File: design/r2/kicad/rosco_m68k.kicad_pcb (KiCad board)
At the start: 4 copper layers, 160 x 100 mm, 84 parts, among them IC1 MC68010P10, IC2 ATF16V8BQL-15PU, IC3 ATF16V8BQL-15PU, IC4 MC68901P, IC5 ATF16V8BQL-15PU, IC6 74174N, IC7 74LS93, IC8 555N, IC9 74LS01N, J1 PWR, J2 Conn_01x06, J3 Conn_02x32_Odd_Even, J4 Conn_01x06, J5 GPIO-PANEL, Q1 3.6864MHz, Q2 5H8ET-10.000, Q3 5H8ET-4.000, U1 AT28C256-15PU, U2 AT28C256-15PU, U3 AS6C4008-55PCN, U4 AS6C4008-55PCN

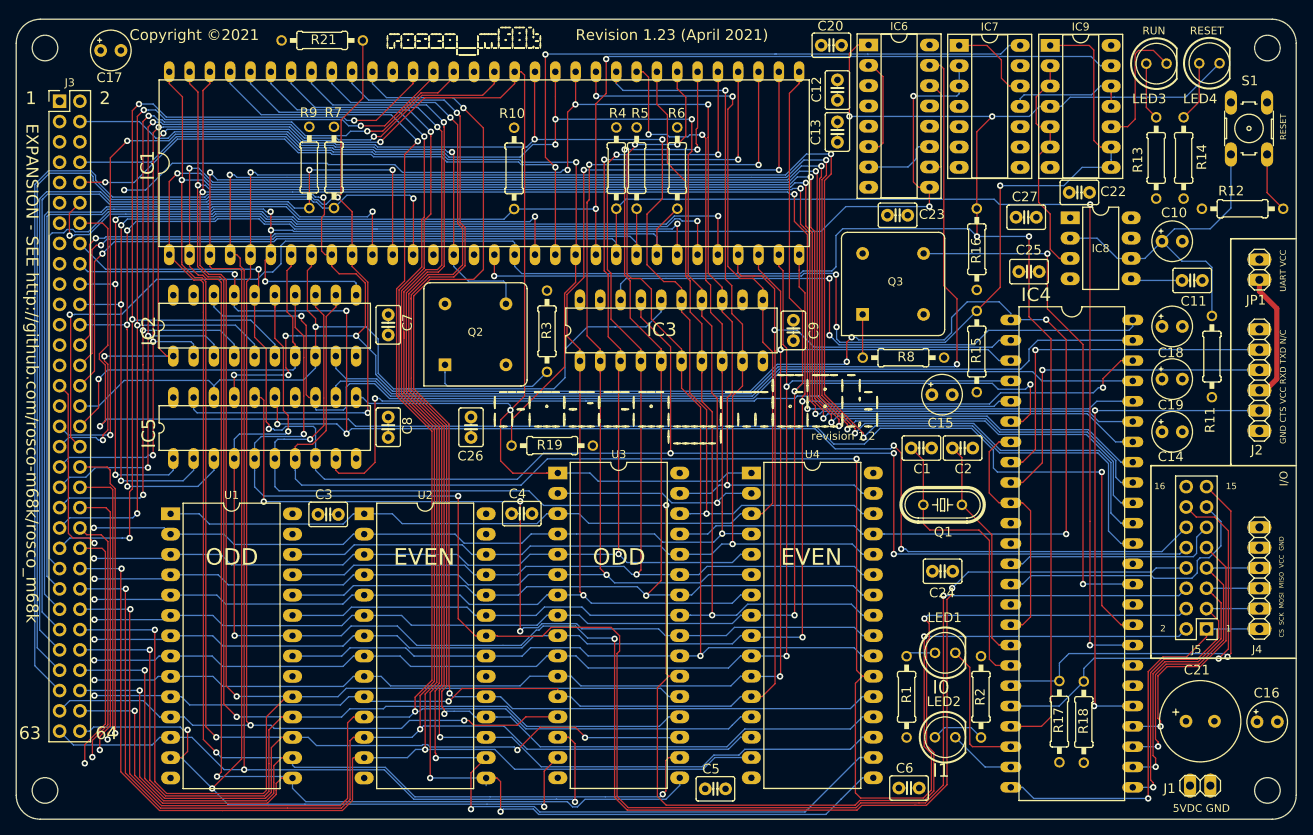
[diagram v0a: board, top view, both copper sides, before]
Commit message: Schematic / GAL tweaks and do layout
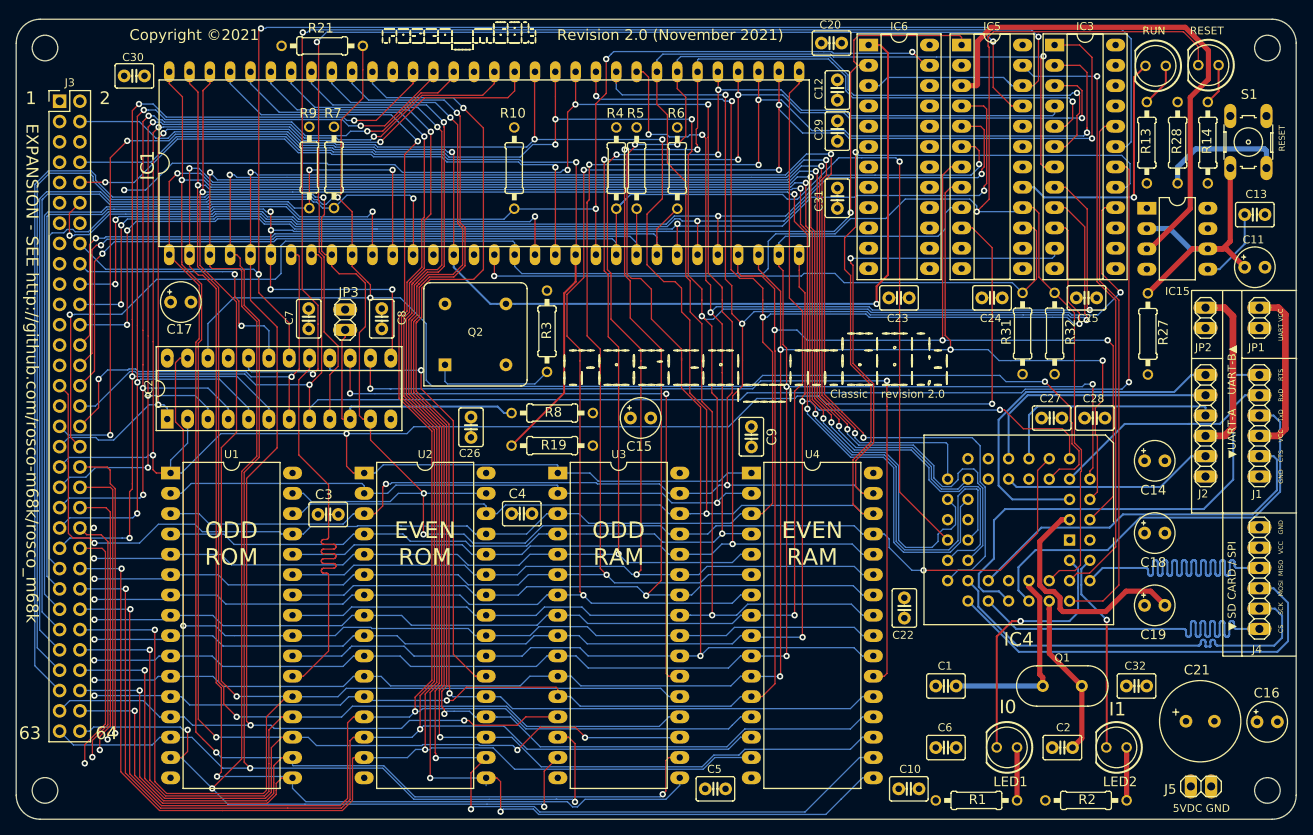
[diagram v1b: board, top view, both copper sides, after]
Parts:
- removed IC7: 74LS93, Package_DIP:DIP-14_W7.62mm_Socket_LongPads
- removed IC8: 555N, Package_DIP:DIP-8_W7.62mm_LongPads
- removed IC9: 74LS01N, Package_DIP:DIP-14_W7.62mm_Socket_LongPads
- removed the LED3 at (210.4, 60.6)
- removed the LED4 at (217.1, 60.6)
- removed Q3: 5H8ET-4.000, Oscillator:Oscillator_DIP-8
- removed R11: 2K2, rosco_m68k:0207_10
- removed R12: 270R, rosco_m68k:0207_10
- removed R15, R16, R17, R18: 4K7, rosco_m68k:0207_10
- removed the REF** at (92.2, 76.3)
- removed the REF** at (153.7, 104.2)
- added C28: 100nF, rosco_m68k:C2.5-3, F.Cu at (202.7, 105.0)
- added C29: 100nF, rosco_m68k:C2.5-3, F.Cu at (170.6, 69.1)
- added C30: 100nF, rosco_m68k:C2.5-3, F.Cu at (82.7, 62.2)
- added C31: 100nF, rosco_m68k:C2.5-3, F.Cu at (170.6, 77.5)
- added C32: 100nF, rosco_m68k:C2.5-3, F.Cu at (207.9, 138.4)
- added IC15: 555N, Package_DIP:DIP-8_W7.62mm_LongPads, F.Cu at (209.2, 78.7)
- added JP2: Jumper, rosco_m68k:1X02, F.Cu at (216.6, 92.4)
- added JP3: Jumper, rosco_m68k:1X02, F.Cu at (109.0, 92.7)
- added LED1: GREEN, rosco_m68k:LED5MM, F.Cu at (191.7, 146.1)
- added LED2: RED, rosco_m68k:LED5MM, F.Cu at (205.4, 146.1)
- added R27: 2K2, rosco_m68k:0207_10, F.Cu at (209.4, 94.4)
- added R28: 270R, rosco_m68k:0207_10, F.Cu at (213.1, 70.5)
- added R31: 4K7, rosco_m68k:0207_10, F.Cu at (193.7, 94.4)
- added R32: 4K7, rosco_m68k:0207_10, F.Cu at (197.7, 94.4)
- added REF**: WEEE-Logo_5.6x8mm_SilkScreen, Symbol:WEEE-Logo_5.6x8mm_SilkScreen, B.Cu at (92.2, 76.9)
- C1, C2: value 33pF -> 7pF
- C10: value 100uF -> 100nF; footprint rosco_m68k:E2,5-5 -> rosco_m68k:C2.5-3
- C11: value 100nF -> 100uF; footprint rosco_m68k:C2.5-3 -> rosco_m68k:E2,5-5
- IC2, IC5: footprint rosco_m68k:DIL20 -> Package_DIP:DIP-24_W7.62mm_Socket_LongPads
- IC3: value ATF16V8BQL-15PU -> ATF22V10C; footprint rosco_m68k:DIL20 -> Package_DIP:DIP-24_W7.62mm_Socket_LongPads
- IC4: value MC68901P -> XR68C681CJTR-F; footprint rosco_m68k:DIL48 -> Package_LCC:PLCC-44_THT-Socket
- IC6: value 74174N -> ATF22V10C; footprint Package_DIP:DIP-16_W7.62mm_Socket_LongPads -> Package_DIP:DIP-24_W7.62mm_Socket_LongPads
- J1: value PWR -> UART_A; footprint rosco_m68k:1X02 -> rosco_m68k:1X06
- J2: value Conn_01x06 -> UART_B
- J5: value GPIO-PANEL -> PWR; footprint Connector_PinHeader_2.54mm:PinHeader_2x08_P2.54mm_Vertical -> rosco_m68k:1X02
- JP1: value FTDI POWER -> Jumper
- Q1: value 3.6864MHz -> Crystal; footprint rosco_m68k:HC49_S -> Crystal:Crystal_HC49-4H_Vertical
- R21: value 2K2 -> 1K2
- U1, U2: value AT28C256-15PU -> SST39SF040; footprint Package_DIP:DIP-28_W15.24mm_LongPads -> Package_DIP:DIP-32_W15.24mm_LongPads
- moved IC5 99.4 mm to (186.1, 58.3)
- moved LED4 90.2 mm to (216.9, 60.8), turned to 180 degrees
- moved LED3 77.9 mm to (210.3, 60.9), turned to 180 degrees
- moved C10 76.0 mm to (179.5, 151.3), turned to 180 degrees
- moved IC3 59.7 mm to (197.7, 58.3)
- moved C22 56.4 mm to (178.9, 128.7), turned to 90 degrees
- moved C13 53.2 mm to (222.7, 79.5), turned to 180 degrees
- moved R8 44.4 mm to (134.9, 104.3)
- moved J1 43.1 mm to (223.3, 108.4), turned to 90 degrees
- moved C2 39.5 mm to (198.7, 146.1), turned to 180 degrees
- moved C15 37.8 mm to (145.9, 104.9)
- moved C24 34.7 mm to (189.9, 89.9)
- moved C17 32.6 mm to (88.5, 90.5)
- moved C1 29.9 mm to (184.1, 138.4)
- moved C19 28.4 mm to (210.2, 128.4)
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- renumbered LED1 to LED3, LED2 to LED4
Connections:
- net /Expansion/A20 renamed A20
- net /Expansion/A21 renamed A21
- net /Expansion/A22 renamed A22
- net /Expansion/A23 renamed A23
- C1 pad 1: Net-(C1-Pad1) -> GND
- C1 pad 2: GND -> Net-(C1-Pad2)
- C13 pad 2: GND -> Net-(C13-Pad2)
- IC1 pad 1: /Expansion/D4 -> D4
- IC1 pad 2: /Expansion/D3 -> D3
- IC1 pad 29: /Expansion/A1 -> A1
- IC1 pad 3: /Expansion/D2 -> D2
- IC1 pad 30: /Expansion/A2 -> A2
- IC1 pad 31: /Expansion/A3 -> A3
- IC1 pad 32: /Expansion/A4 -> A4
- IC1 pad 33: /Expansion/A5 -> A5
- IC1 pad 34: /Expansion/A6 -> A6
- IC1 pad 35: /Expansion/A7 -> A7
- IC1 pad 36: /Expansion/A8 -> A8
- IC1 pad 37: /Expansion/A9 -> A9
- IC1 pad 38: /Expansion/A10 -> A10
- IC1 pad 39: /Expansion/A11 -> A11
- IC1 pad 4: /Expansion/D1 -> D1
- IC1 pad 40: /Expansion/A12 -> A12
- IC1 pad 41: /Expansion/A13 -> A13
- IC1 pad 42: /Expansion/A14 -> A14
- IC1 pad 43: /Expansion/A15 -> A15
- IC1 pad 44: /Expansion/A16 -> A16
- IC1 pad 45: /Expansion/A17 -> A17
- IC1 pad 46: /Expansion/A18 -> A18
- IC1 pad 47: /Expansion/A19 -> A19
- IC1 pad 5: /Expansion/D0 -> D0
- IC1 pad 54: /Expansion/D15 -> D15
- IC1 pad 55: /Expansion/D14 -> D14
- IC1 pad 56: /Expansion/D13 -> D13
- IC1 pad 57: /Expansion/D12 -> D12
- IC1 pad 58: /Expansion/D11 -> D11
- IC1 pad 59: /Expansion/D10 -> D10
- IC1 pad 60: /Expansion/D9 -> D9
- IC1 pad 61: /Expansion/D8 -> D8
- IC1 pad 62: /Expansion/D7 -> D7
- IC1 pad 63: /Expansion/D6 -> D6
- IC1 pad 64: /Expansion/D5 -> D5
- IC2 pad 1: /Expansion/A18 -> A18
- IC2 pad 10: GND -> LGEXP
- IC2 pad 11: AS -> RW
- IC2 pad 12: EVENRAMSEL -> GND
- IC2 pad 13: ODDRAMSEL -> AS
- IC2 pad 14: EVENROMSEL -> EVENRAMSEL
- IC2 pad 15: ODDROMSEL -> ODDRAMSEL
- IC2 pad 16: IOSEL -> EVENROMSEL
- IC2 pad 17: EXPSEL -> ODDROMSEL
- IC2 pad 18: IACK -> IOSEL
- IC2 pad 19: Net-(IC2-Pad19) -> EXPSEL
- IC2 pad 2: /Expansion/A19 -> A19
- IC2 pad 20: VCC -> ANYIACK
- IC3 pad 1: /Expansion/A6 -> A6
- IC3 pad 10: GND -> A15
- IC3 pad 11: /Expansion/A15 -> A16
- IC3 pad 12: Net-(IC3-Pad12) -> GND
- IC3 pad 13: /Expansion/A16 -> Net-(IC3-Pad13)
- IC3 pad 14: /Expansion/A17 -> Net-(IC3-Pad14)
- IC3 pad 15: /Expansion/A18 -> Net-(IC3-Pad15)
- IC3 pad 16: LDS -> A17
- IC3 pad 17: IOSEL -> A18
- IC3 pad 18: MFPSEL -> LDS
- IC3 pad 19: Net-(IC3-Pad19) -> IOSEL
- IC3 pad 2: /Expansion/A7 -> A7
- IC3 pad 20: VCC -> DUASEL
- IC3 pad 3: /Expansion/A8 -> A8
- IC3 pad 4: /Expansion/A9 -> A9
- IC3 pad 5: /Expansion/A10 -> A10
- IC3 pad 6: /Expansion/A11 -> A11
- IC3 pad 7: /Expansion/A12 -> A12
- IC3 pad 8: /Expansion/A13 -> A13
- IC3 pad 9: /Expansion/A14 -> A14
- IC4 pad 1: RW -> Net-(IC4-Pad1)
- IC4 pad 10: Net-(IC4-Pad10) -> DTACK
- IC4 pad 11: VCC -> RXDB
- IC4 pad 12: (no net) -> Net-(IC4-Pad12)
- IC4 pad 13: TAO -> TXDB
- IC4 pad 14: TBO -> CTSB
- IC4 pad 16: Net-(IC4-Pad10) -> Net-(IC4-Pad16)
- IC4 pad 17: Net-(C2-Pad1) -> Net-(IC4-Pad17)
- IC4 pad 18: Net-(C1-Pad1) -> D1
- IC4 pad 19: TAI -> D3
- IC4 pad 2: /Expansion/A1 -> A1
- IC4 pad 20: TBI -> D5
- IC4 pad 21: RESET -> D7
- IC4 pad 22: Net-(IC4-Pad22) -> GND
- IC4 pad 24: GPIO1 -> IPL2
- IC4 pad 25: GPIO2 -> D6
- IC4 pad 26: GPIO3 -> D4
- IC4 pad 27: GPIO4 -> D2
- IC4 pad 28: GPIO5 -> D0
- IC4 pad 29: Net-(IC4-Pad29) -> SPIMOSI
- IC4 pad 3: /Expansion/A2 -> GND
- IC4 pad 30: Net-(IC4-Pad30) -> SPICLK
- IC4 pad 31: Net-(IC4-Pad31) -> SPICS
- IC4 pad 32: IPL2 -> CTSA
- IC4 pad 33: IEO -> TXDA
- IC4 pad 34: GND -> Net-(IC4-Pad34)
- IC4 pad 35: MFPCLK -> RXDA
- IC4 pad 36: GND -> Net-(C1-Pad2)
- IC4 pad 37: /Expansion/D0 -> Net-(C2-Pad1)
- IC4 pad 38: /Expansion/D1 -> RESET
- IC4 pad 39: /Expansion/D2 -> DUASEL
- IC4 pad 4: /Expansion/A3 -> A2
- IC4 pad 40: /Expansion/D3 -> SPIMISO
- IC4 pad 41: /Expansion/D4 -> DUAIACK
- IC4 pad 42: /Expansion/D5 -> Net-(IC4-Pad42)
- IC4 pad 43: /Expansion/D6 -> Net-(IC4-Pad43)
- IC4 pad 44: /Expansion/D7 -> VCC
- IC4 pad 5: /Expansion/A4 -> RTSB
- IC4 pad 6: /Expansion/A5 -> A3
- IC4 pad 7: Net-(IC4-Pad10) -> A4
- IC4 pad 8: /Main_Bus/UARTTX -> RTSA
- IC4 pad 9: /Main_Bus/UARTRX -> RW
- IC5 pad 1: FC0 -> AS
- IC5 pad 10: GND -> A19
- IC5 pad 11: /Expansion/A19 -> Net-(IC5-Pad11)
- IC5 pad 12: MFPDS -> GND
- IC5 pad 13: IACK -> Net-(IC5-Pad13)
- IC5 pad 15: EXPSEL -> HALT
- IC5 pad 16: RAMOE -> RESET
- IC5 pad 17: RW -> RUNLED
- IC5 pad 18: LDS -> Net-(IC5-Pad18)
- IC5 pad 19: DTACK -> Net-(IC5-Pad19)
- IC5 pad 2: FC1 -> Net-(IC5-Pad2)
- IC5 pad 20: VCC -> Net-(IC5-Pad20)
- IC5 pad 3: FC2 -> HWRST
- IC5 pad 4: ODDROMSEL -> FC2
- IC5 pad 5: EVENROMSEL -> FC1
- IC5 pad 6: ODDRAMSEL -> FC0
- IC5 pad 7: EVENRAMSEL -> A1
- IC5 pad 8: IOSEL -> A2
- IC5 pad 9: IODTACK -> A3
- IC6 pad 1: RESET -> CLK
- IC6 pad 12: Net-(IC6-Pad12) -> GND
- IC6 pad 14: Net-(IC6-Pad10) -> Net-(IC6-Pad14)
- IC6 pad 15: BOOT -> Net-(IC6-Pad15)
- IC6 pad 16: VCC -> Net-(IC6-Pad16)
- IC6 pad 2: Net-(IC6-Pad2) -> AS
- IC6 pad 3: VCC -> ANYIACK
- IC6 pad 4: GND -> Net-(IC6-Pad4)
- IC6 pad 6: Net-(IC6-Pad2) -> Net-(IC6-Pad6)
- IC6 pad 7: Net-(IC6-Pad11) -> Net-(IC6-Pad7)
- IC6 pad 8: GND -> Net-(IC6-Pad8)
- IC6 pad 9: AS -> Net-(IC6-Pad9)
- J1 pad 1: VCC -> GND
- J1 pad 2: GND -> CTSA
- J2 pad 2: Net-(IC4-Pad29) -> CTSB
- J2 pad 3: Net-(J2-Pad3) -> VCCUB
- J2 pad 4: /Main_Bus/UARTRX -> RXDB
- J2 pad 5: /Main_Bus/UARTTX -> TXDB
- J2 pad 6: Net-(J2-Pad6) -> RTSB
- J3 pad 1: /Expansion/A1 -> A1
- J3 pad 11: /Expansion/A6 -> A6
- J3 pad 13: /Expansion/A7 -> A7
- J3 pad 14: IEO -> Net-(J3-Pad14)
- J3 pad 15: /Expansion/A8 -> A8
- J3 pad 17: /Expansion/A9 -> A9
- J3 pad 19: /Expansion/A10 -> A10
- J3 pad 21: /Expansion/A11 -> A11
- J3 pad 23: /Expansion/A12 -> A12
- J3 pad 25: /Expansion/A13 -> A13
- J3 pad 27: /Expansion/A14 -> A14
- J3 pad 29: /Expansion/A15 -> A15
- J3 pad 3: /Expansion/A2 -> A2
- J3 pad 31: /Expansion/A16 -> A16
- J3 pad 33: /Expansion/A17 -> A17
- J3 pad 35: /Expansion/A18 -> A18
- J3 pad 37: /Expansion/A19 -> A19
- J3 pad 38: /Expansion/D15 -> D15
- J3 pad 40: /Expansion/D14 -> D14
- J3 pad 42: /Expansion/D13 -> D13
- J3 pad 44: /Expansion/D12 -> D12
- J3 pad 46: /Expansion/D11 -> D11
- J3 pad 48: /Expansion/D10 -> D10
- J3 pad 5: /Expansion/A3 -> A3
- J3 pad 50: /Expansion/D9 -> D9
- J3 pad 52: /Expansion/D8 -> D8
- J3 pad 54: /Expansion/D7 -> D7
- J3 pad 56: /Expansion/D6 -> D6
- J3 pad 58: /Expansion/D5 -> D5
- J3 pad 60: /Expansion/D4 -> D4
- J3 pad 61: /Expansion/D0 -> D0
- J3 pad 62: /Expansion/D3 -> D3
- J3 pad 63: /Expansion/D1 -> D1
- J3 pad 64: /Expansion/D2 -> D2
- J3 pad 7: /Expansion/A4 -> A4
- J3 pad 9: /Expansion/A5 -> A5
- J4 pad 1: GPIO1 -> SPICS
- J4 pad 2: GPIO2 -> SPICLK
- J4 pad 3: GPIO3 -> SPIMOSI
- J4 pad 4: GPIO4 -> SPIMISO
- J5 pad 1: GPIO1 -> VCC
- J5 pad 2: EVENRAMSEL -> GND
- JP1 pad 1: VCC -> VCCUA
- JP1 pad 2: Net-(J2-Pad3) -> VCC
- LED3 pad A: Net-(LED1-PadA) -> Net-(LED3-PadA)
- LED3 pad K: Net-(IC4-Pad22) -> RUNLED
- LED4 pad A: Net-(LED2-PadA) -> Net-(LED4-PadA)
- LED4 pad K: Net-(IC4-Pad23) -> RESET
- Q1 pad 1: Net-(C1-Pad1) -> Net-(C1-Pad2)
- R21 pad 1: DTACK -> VCC
- R21 pad 2: VCC -> DTACK
- R8 pad 2: Net-(Q3-Pad1) -> LGEXP
- S1 pad 1: Net-(C10-Pad+) -> Net-(C11-Pad+)
- U1 pad 1: /Expansion/A15 -> A19
- U1 pad 10: /Expansion/A1 -> A3
- U1 pad 11: /Expansion/D0 -> A2
- U1 pad 12: /Expansion/D1 -> A1
- U1 pad 13: /Expansion/D2 -> D0
- U1 pad 14: GND -> D1
- U1 pad 15: /Expansion/D3 -> D2
- U1 pad 16: /Expansion/D4 -> GND
- U1 pad 17: /Expansion/D5 -> D3
- U1 pad 18: /Expansion/D6 -> D4
- U1 pad 19: /Expansion/D7 -> D5
- U1 pad 2: /Expansion/A13 -> A17
- U1 pad 20: GND -> D6
- U1 pad 21: /Expansion/A11 -> D7
- U1 pad 23: /Expansion/A12 -> A11
- U1 pad 24: /Expansion/A10 -> WR
- U1 pad 25: /Expansion/A9 -> A12
- U1 pad 26: /Expansion/A14 -> A10
- U1 pad 27: VCC -> A9
- U1 pad 28: VCC -> A14
- U1 pad 3: /Expansion/A8 -> A16
- U1 pad 4: /Expansion/A7 -> A13
- U1 pad 5: /Expansion/A6 -> A8
- U1 pad 6: /Expansion/A5 -> A7
- U1 pad 7: /Expansion/A4 -> A6
- U1 pad 8: /Expansion/A3 -> A5
- U1 pad 9: /Expansion/A2 -> A4
- U2 pad 1: /Expansion/A15 -> A19
- U2 pad 10: /Expansion/A1 -> A3
- U2 pad 11: /Expansion/D8 -> A2
- U2 pad 12: /Expansion/D9 -> A1
- U2 pad 13: /Expansion/D10 -> D8
- U2 pad 14: GND -> D9
- U2 pad 15: /Expansion/D11 -> D10
- U2 pad 16: /Expansion/D12 -> GND
- U2 pad 17: /Expansion/D13 -> D11
- U2 pad 18: /Expansion/D14 -> D12
- U2 pad 19: /Expansion/D15 -> D13
- U2 pad 2: /Expansion/A13 -> A17
- U2 pad 20: GND -> D14
- U2 pad 21: /Expansion/A11 -> D15
- U2 pad 23: /Expansion/A12 -> A11
- U2 pad 24: /Expansion/A10 -> WR
- U2 pad 25: /Expansion/A9 -> A12
- U2 pad 26: /Expansion/A14 -> A10
- U2 pad 27: VCC -> A9
- U2 pad 28: VCC -> A14
- U2 pad 3: /Expansion/A8 -> A16
- U2 pad 4: /Expansion/A7 -> A13
- U2 pad 5: /Expansion/A6 -> A8
- U2 pad 6: /Expansion/A5 -> A7
- U2 pad 7: /Expansion/A4 -> A6
- U2 pad 8: /Expansion/A3 -> A5
- U2 pad 9: /Expansion/A2 -> A4
- U3 pad 1: /Expansion/A19 -> A19
- U3 pad 10: /Expansion/A3 -> A3
- U3 pad 11: /Expansion/A2 -> A2
- U3 pad 12: /Expansion/A1 -> A1
- U3 pad 13: /Expansion/D0 -> D0
- U3 pad 14: /Expansion/D1 -> D1
- U3 pad 15: /Expansion/D2 -> D2
- U3 pad 17: /Expansion/D3 -> D3
- U3 pad 18: /Expansion/D4 -> D4
- U3 pad 19: /Expansion/D5 -> D5
- U3 pad 2: /Expansion/A17 -> A17
- U3 pad 20: /Expansion/D6 -> D6
- U3 pad 21: /Expansion/D7 -> D7
- U3 pad 23: /Expansion/A11 -> A11
- U3 pad 24: RAMOE -> WR
- U3 pad 25: /Expansion/A12 -> A12
- U3 pad 26: /Expansion/A10 -> A10
- U3 pad 27: /Expansion/A9 -> A9
- U3 pad 28: /Expansion/A14 -> A14
- U3 pad 3: /Expansion/A15 -> A15
- U3 pad 30: /Expansion/A18 -> A18
- U3 pad 31: /Expansion/A16 -> A16
- U3 pad 4: /Expansion/A13 -> A13
- U3 pad 5: /Expansion/A8 -> A8
- U3 pad 6: /Expansion/A7 -> A7
- U3 pad 7: /Expansion/A6 -> A6
- U3 pad 8: /Expansion/A5 -> A5
- U3 pad 9: /Expansion/A4 -> A4
- U4 pad 1: /Expansion/A19 -> A19
- U4 pad 10: /Expansion/A3 -> A3
- U4 pad 11: /Expansion/A2 -> A2
- U4 pad 12: /Expansion/A1 -> A1
- U4 pad 13: /Expansion/D8 -> D8
- U4 pad 14: /Expansion/D9 -> D9
- U4 pad 15: /Expansion/D10 -> D10
- U4 pad 17: /Expansion/D11 -> D11
- U4 pad 18: /Expansion/D12 -> D12
- U4 pad 19: /Expansion/D13 -> D13
- U4 pad 2: /Expansion/A17 -> A17
- U4 pad 20: /Expansion/D14 -> D14
- U4 pad 21: /Expansion/D15 -> D15
- U4 pad 23: /Expansion/A11 -> A11
- U4 pad 24: RAMOE -> WR
- U4 pad 25: /Expansion/A12 -> A12
- U4 pad 26: /Expansion/A10 -> A10
- U4 pad 27: /Expansion/A9 -> A9
- U4 pad 28: /Expansion/A14 -> A14
- U4 pad 3: /Expansion/A15 -> A15
- U4 pad 30: /Expansion/A18 -> A18
- U4 pad 31: /Expansion/A16 -> A16
- U4 pad 4: /Expansion/A13 -> A13
- U4 pad 5: /Expansion/A8 -> A8
- U4 pad 6: /Expansion/A7 -> A7
- U4 pad 7: /Expansion/A6 -> A6
- U4 pad 8: /Expansion/A5 -> A5
- U4 pad 9: /Expansion/A4 -> A4
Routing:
- net D6: track 0.00 -> 344.1 mm, vias 0 -> 5
- net /Expansion/D5: track 343.8 -> 0.00 mm, vias 7 -> 0
- net A18: track 0.00 -> 341.1 mm, vias 0 -> 6
- net /Expansion/D6: track 338.9 -> 0.00 mm, vias 5 -> 0
- net D5: track 0.00 -> 337.5 mm, vias 0 -> 7
- net /Expansion/D7: track 336.9 -> 0.00 mm, vias 5 -> 0
- net /Expansion/D4: track 336.0 -> 0.00 mm, vias 6 -> 0
- net D7: track 0.00 -> 335.2 mm, vias 0 -> 5
- net /Expansion/D3: track 333.8 -> 0.00 mm, vias 5 -> 0
- net D4: track 0.00 -> 331.1 mm, vias 0 -> 6
- net A16: track 0.00 -> 323.8 mm, vias 0 -> 7
- net A1: track 0.00 -> 323.5 mm, vias 0 -> 5
- net A17: track 0.00 -> 320.0 mm, vias 0 -> 8
- net /Expansion/D2: track 312.7 -> 0.00 mm, vias 6 -> 0
- net D3: track 0.00 -> 312.4 mm, vias 0 -> 5
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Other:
- board text added: "CS"
- board text added: "CTS"
- board text added: "Classic"
- board text added: "EVEN RAM"
- board text added: "EVEN ROM"
- board text added: "GND"
- board text added: "MISO"
- board text added: "MOSI"
- board text added: "ODD RAM"
- board text added: "ODD ROM"
- board text added: "RTS"
- board text added: "Revision 2.0 (November 2021)"
- board text added: "RxD"
- board text added: "SCK"
- board text added: "TxD"
- board text added: "VCC"
- board text added: "revision 2.0"
- board text added: "rosco_m68k classic"
- board text added: "▼ SD CARD / SPI"
- board text added: "▼UART-A UART-B▲"
- board text removed: "15"
- board text removed: "16"
- board text removed: "CS SCK MOSI MISO VCC GND"
- board text removed: "EVEN"
- board text removed: "First Anniversary Edition"
- board text removed: "GND CTS VCC RXD TXD N/C"
- board text removed: "I/O"
- board text removed: "ODD"
- board text removed: "Revision 1.23 (April 2021)"
- board text removed: "revision 1.2"
- board text removed: "revision 1.23"
- board text removed: "rosco_m68k"

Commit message: Add ROM write-enable jumper and tidy up
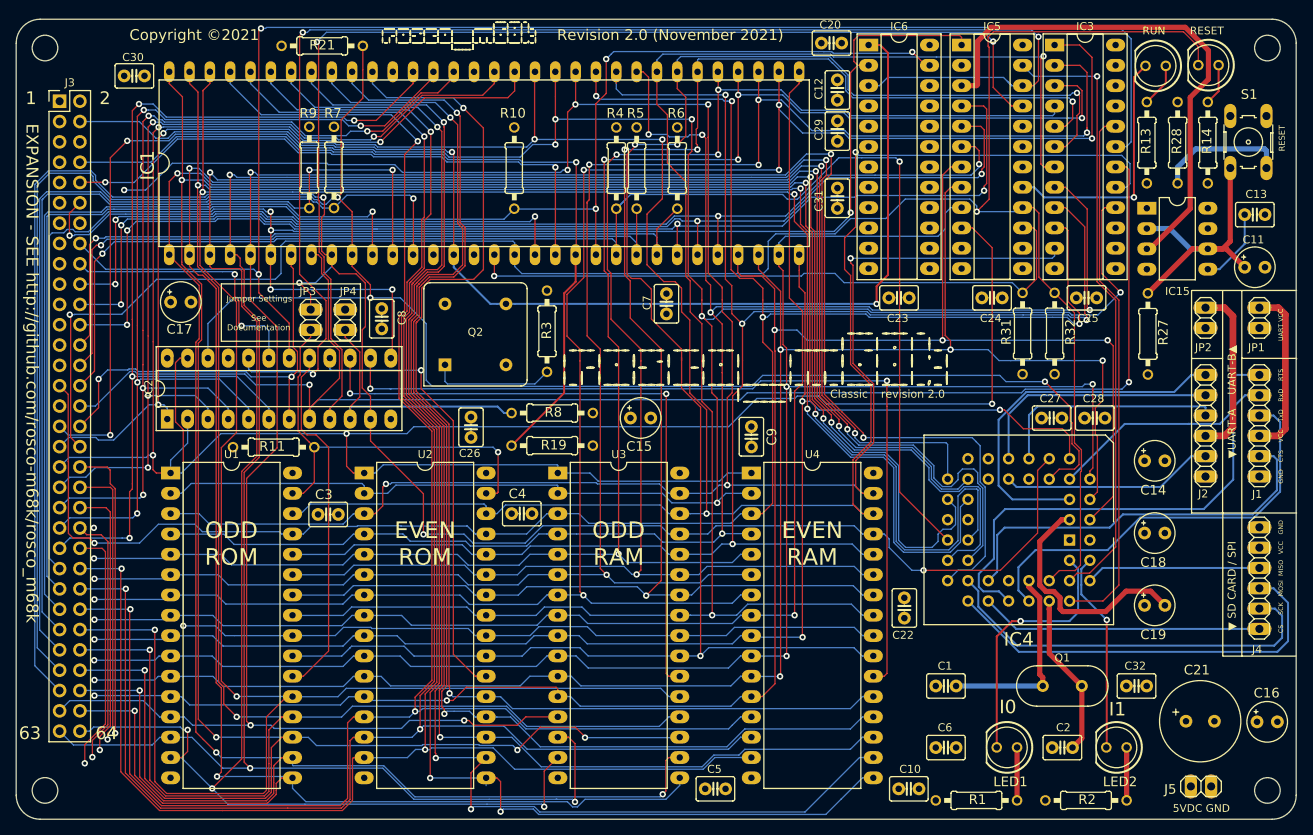
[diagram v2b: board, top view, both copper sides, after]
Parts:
- added JP4: Jumper, rosco_m68k:1X02, F.Cu at (109.0, 92.7)
- added R11: 10K, rosco_m68k:0207_10, F.Cu at (100.1, 108.6)
- moved C7 44.8 mm to (149.2, 90.7)
- moved JP3 4.31 mm to (104.7, 92.7), turned to 270 degrees
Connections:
- JP3 pad 1: LGEXP -> RW
- JP3 pad 2: GND -> ROM_RW
- U1 pad 31: RW -> ROM_RW
- U2 pad 31: RW -> ROM_RW
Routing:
- net ROM_RW: track 0.00 -> 53.6 mm, vias 0 -> 1
- net GND: track 55.3 -> 94.0 mm
- net SPIMISO: track 52.3 -> 21.8 mm
- net SPICS: track 52.3 -> 35.3 mm
- net RW: track 272.6 -> 257.0 mm
- net ODDROMSEL: track 55.2 -> 44.9 mm
- net LDS: track 186.9 -> 193.0 mm
- net CTSA: track 47.0 -> 49.7 mm
- net SPICLK: track 52.5 -> 50.2 mm
- net ANYIACK: track 174.6 -> 175.8 mm
- net UDS: track 53.9 -> 53.2 mm
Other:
- board text added: "Jumper Settings"
- board text added: "See Documentation"

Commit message: Changes requested by @e2k
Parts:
- added J6: Conn_01x04_Male, Connector_PinHeader_2.54mm:PinHeader_1x04_P2.54mm_Vertical, F.Cu at (107.0, 119.6)
- moved C4 34.4 mm to (131.1, 151.3)
- moved C3 34.3 mm to (106.4, 151.3)
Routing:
- net A20: track 113.1 -> 143.6 mm, vias 4 -> 5
- net A21: track 114.8 -> 141.2 mm, vias 4 -> 5
- net A22: track 118.4 -> 142.0 mm, vias 4 -> 5
- net A23: track 123.6 -> 137.2 mm, vias 4 -> 5
- net A13: track 246.9 -> 248.3 mm
- net ODDROMSEL: track 44.9 -> 46.2 mm
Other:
- board text added: "A20"
- board text added: "A21"
- board text added: "A22"
- board text added: "A23"
- board text added: "ADDRESS DECODER"
- board text added: "DUART GLUE LOGIC"
- board text added: "GENERAL GLUE LOGIC"
- board text added: "WATCHDOG"

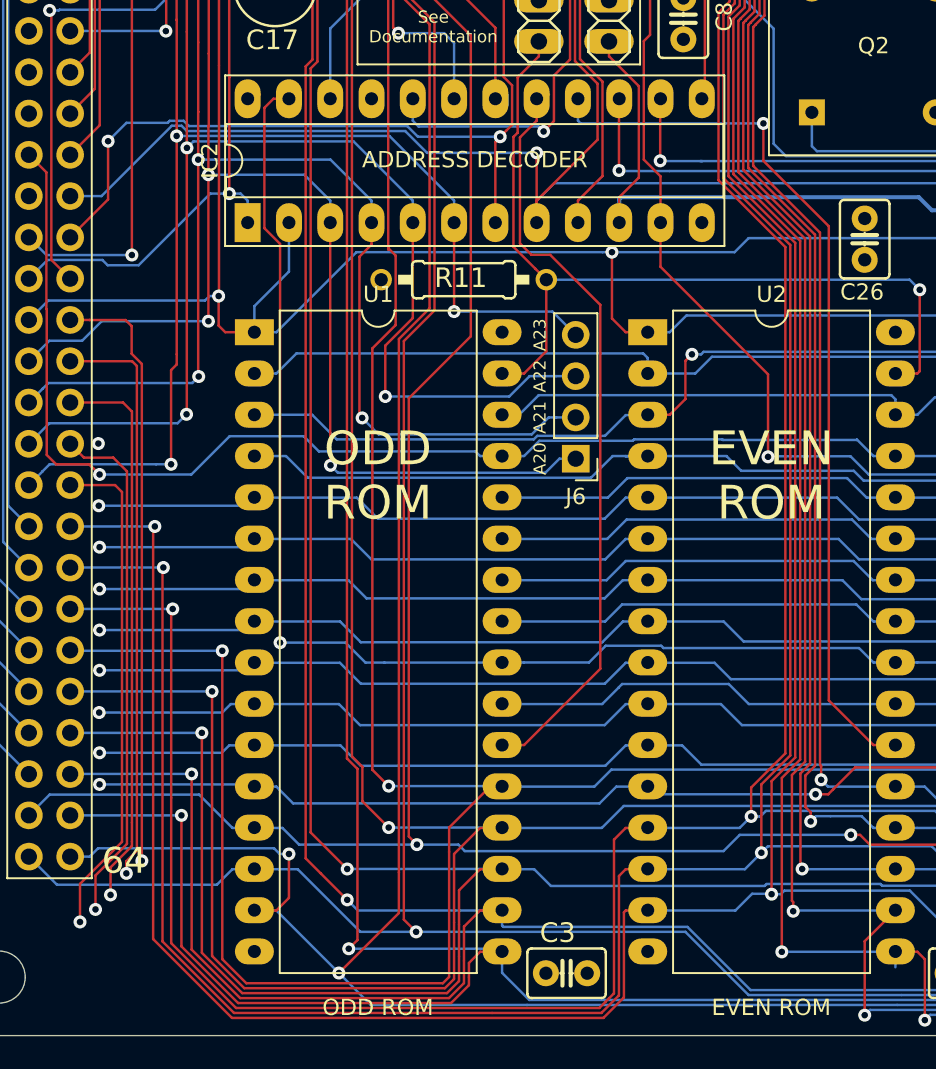
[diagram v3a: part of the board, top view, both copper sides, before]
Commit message: Fix C3 unconnected issue
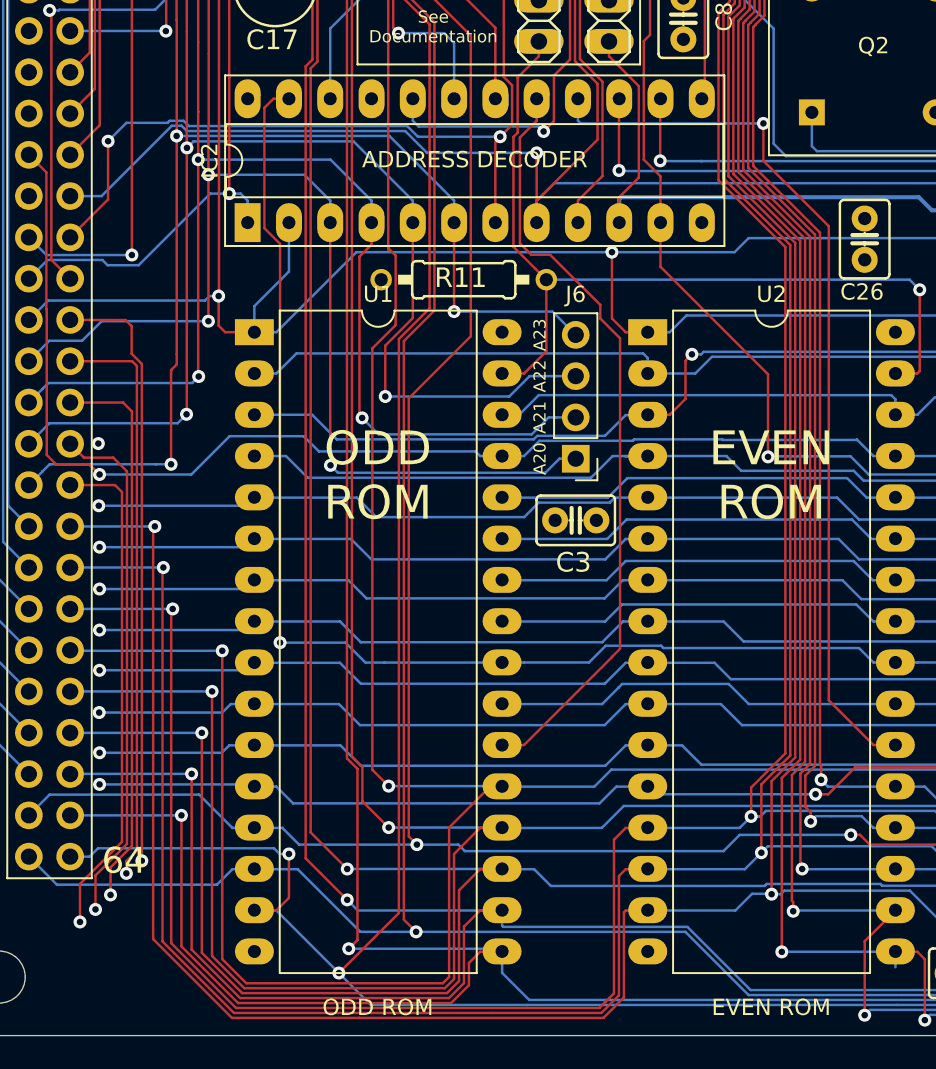
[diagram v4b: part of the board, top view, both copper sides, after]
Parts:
- moved C3 27.9 mm to (107.0, 123.4)
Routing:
- net ODDROMSEL: track 46.2 -> 47.2 mm
